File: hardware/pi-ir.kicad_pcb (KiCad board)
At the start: 2 copper layers, 56 x 35 mm, 10 parts, among them P1 RASPBERRYPI, P2 IROUT0, P3 IRIN, P4 IROUT1, U1 MOSFET-N, U2 MOSFET-N

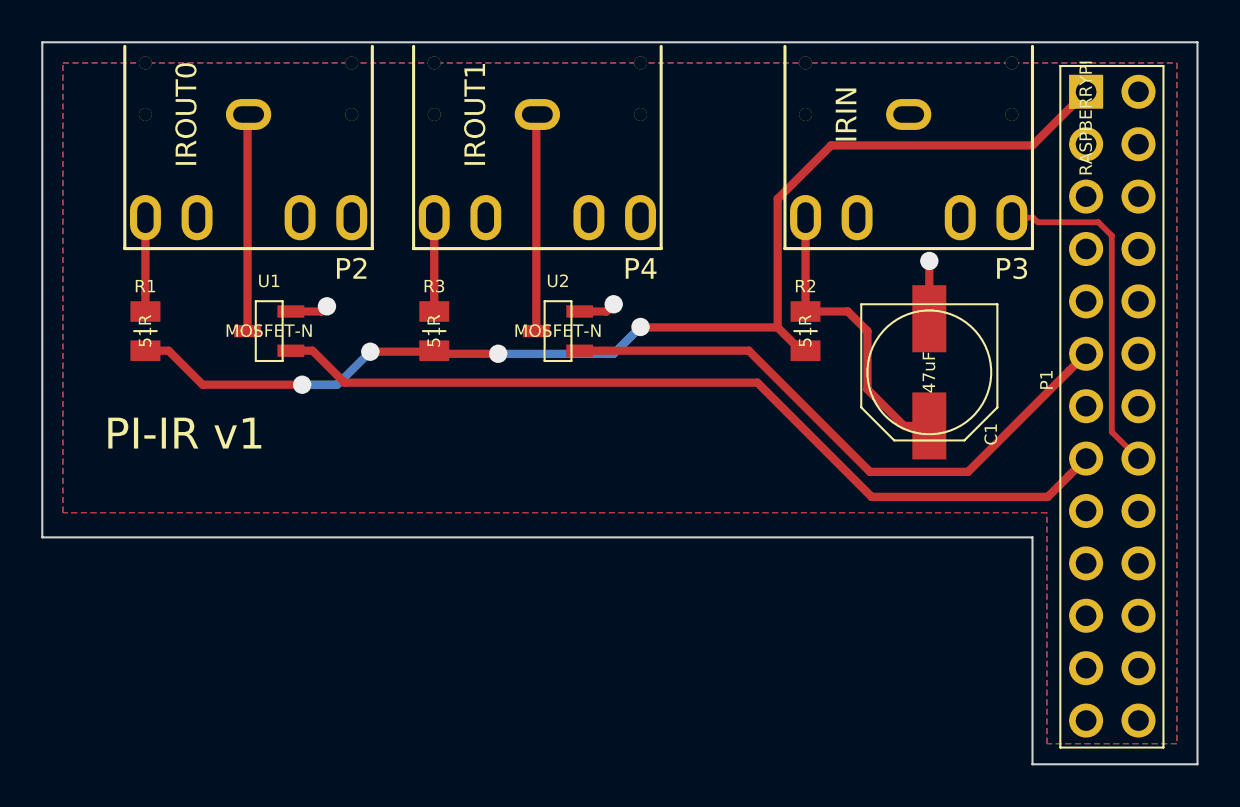
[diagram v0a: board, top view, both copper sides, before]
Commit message: add labels
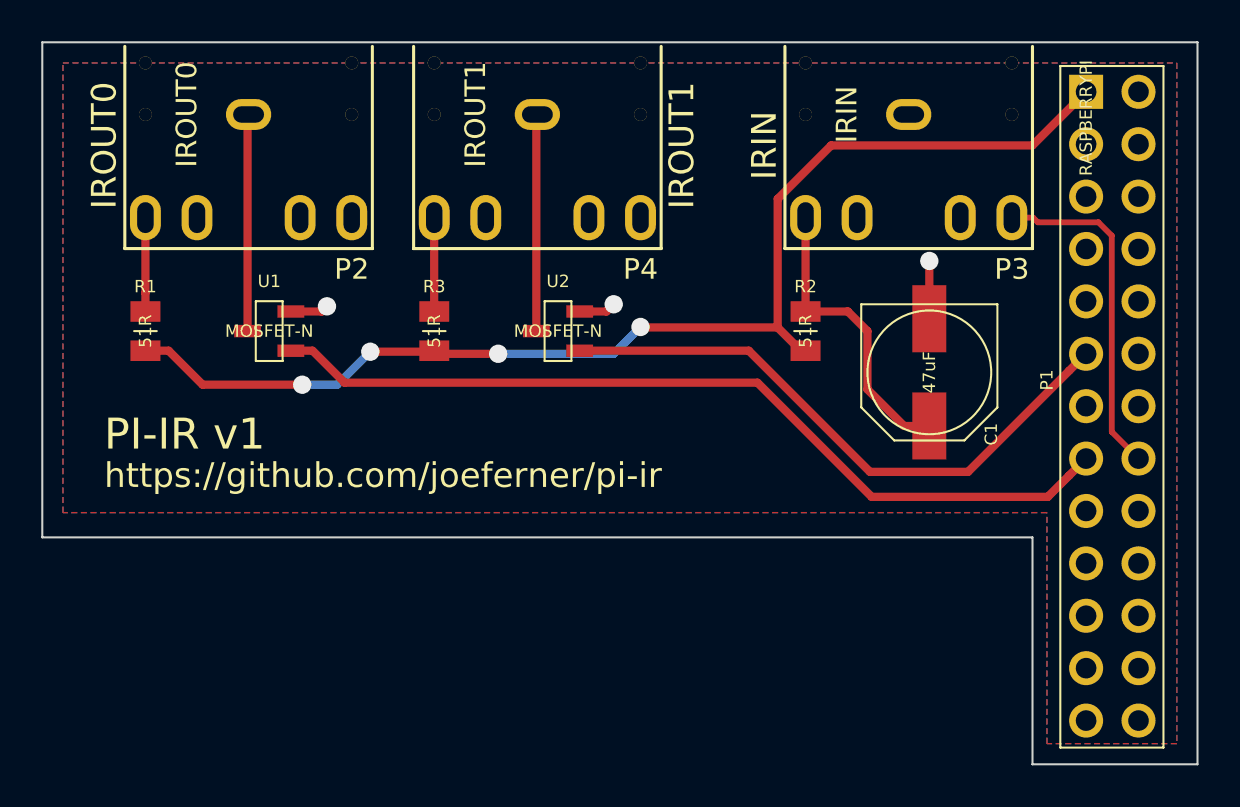
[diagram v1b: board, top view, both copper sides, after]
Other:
- board text added: "IRIN"
- board text added: "IROUT0"
- board text added: "IROUT1"
- board text added: "https://github.com/joeferner/pi-ir"

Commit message: initial v1 try
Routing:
- net +3.3V: track 57.8 -> 59.2 mm

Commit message: v1
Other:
- board text added: "By Joe Ferner"
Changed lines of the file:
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@@
     (area 99.949999 94.68 165.407144 135.050001)
     (thickness 1.6)
-    (drawings 13)
+    (drawings 14)
     (tracks 64)
     (zones 0)
@@
       (net 27 "Net-(P2-Pad2)"))
   )
+  (gr_text "By Joe Ferner" (at 123.6 118.6) (layer B.SilkS)
+    (effects (font (size 1.5 1.5) (thickness 0.3)) (justify mirror))
+  )
   (gr_text IRIN (at 135 105 90) (layer F.SilkS)

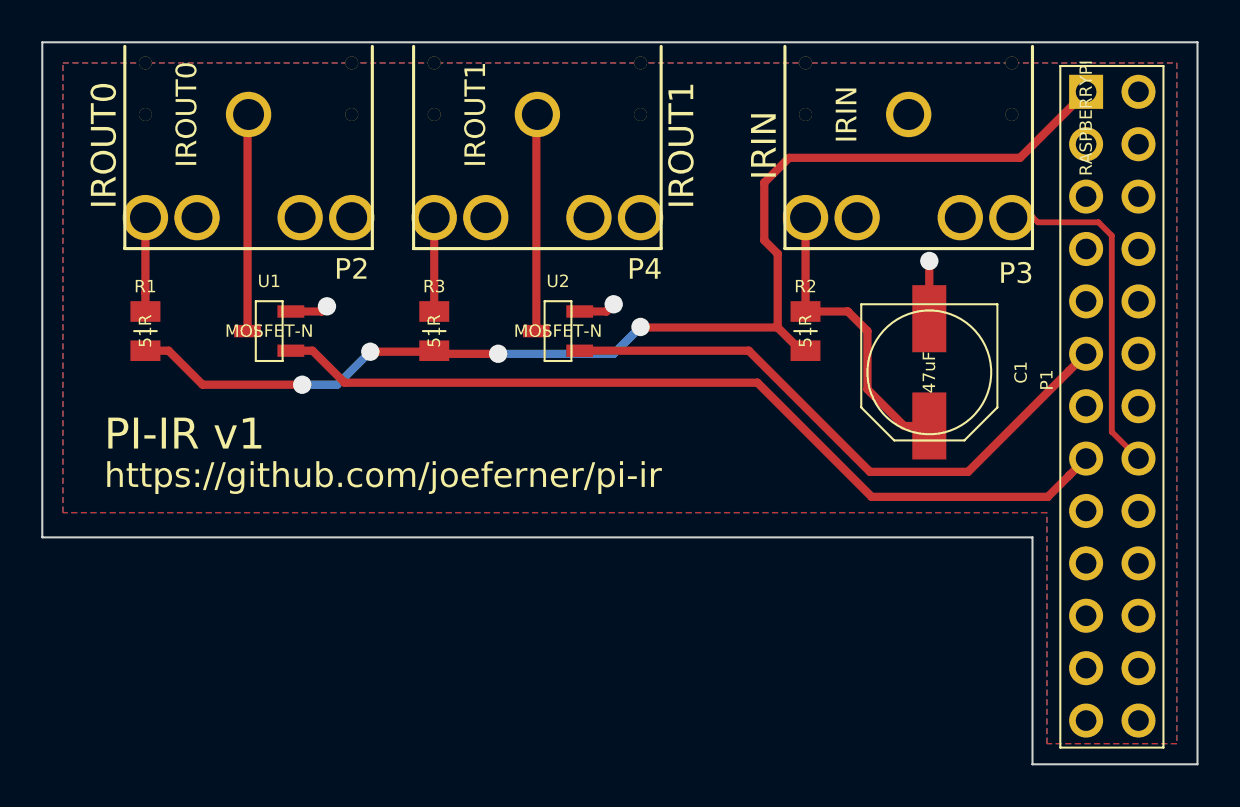
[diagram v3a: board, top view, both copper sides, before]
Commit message: add center hole to audio jack and try to fix drill
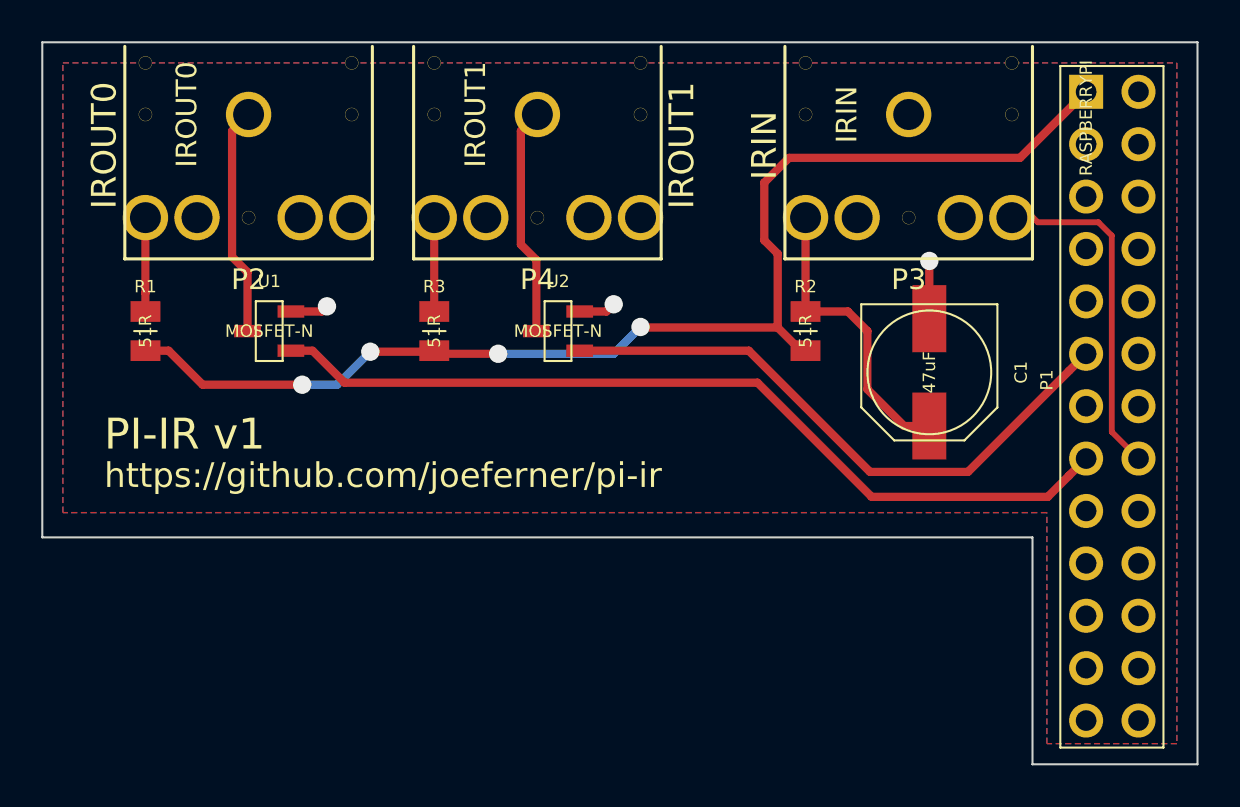
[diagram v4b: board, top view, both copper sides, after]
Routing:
- net Net-(P4-Pad1): track 10.5 -> 11.2 mm
- net Net-(P2-Pad1): track 10.5 -> 11.2 mm

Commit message: update kicad version
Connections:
- P1 pad 25: (no net) -> Net-(P1-Pad25)
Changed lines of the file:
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@@
-(kicad_pcb (version 3) (host pcbnew "(2014-05-22 BZR 4881)-product")
+(kicad_pcb (version 4) (host pcbnew "(2014-jul-16 BZR unknown)-product")
   (general
     (links 16)
@@
     (zones 0)
     (modules 10)
-    (nets 33)
+    (nets 34)
   )
   (page A4)
   (layers
-    (15 F.Cu signal)
-    (0 B.Cu signal)
-    (16 B.Adhes user)
-    (17 F.Adhes user)
-    (18 B.Paste user)
-    (19 F.Paste user)
-    (20 B.SilkS user)
-    (21 F.SilkS user)
-    (22 B.Mask user)
-    (23 F.Mask user)
-    (24 Dwgs.User user)
-    (25 Cmts.User user)
-    (26 Eco1.User user)
-    (27 Eco2.User user)
-    (28 Edge.Cuts user)
+    (0 F.Cu signal)
+    (31 B.Cu signal)
+    (32 B.Adhes user)
+    (33 F.Adhes user)
+    (34 B.Paste user)
+    (35 F.Paste user)
+    (36 B.SilkS user)
+    (37 F.SilkS user)
+    (38 B.Mask user)
+    (39 F.Mask user)
+    (40 Dwgs.User user)
+    (41 Cmts.User user)
+    (42 Eco1.User user)
+    (43 Eco2.User user)
+    (44 Edge.Cuts user)
   )
   (setup
@@
     (visible_elements FFFEFF7F)
     (pcbplotparams
-      (layerselection 284196865)
+      (layerselection 0x00030_80000001)
       (usegerberextensions true)
       (excludeedgelayer false)
@@
   (net 31 "Net-(P2-Pad3)")
   (net 32 "Net-(P4-Pad3)")
+  (net 33 "Net-(P1-Pad25)")
   (net_class Default "This is the default net class."
     (clearance 0.2032)
@@
     (add_net "Net-(P1-Pad23)")
     (add_net "Net-(P1-Pad24)")
+    (add_net "Net-(P1-Pad25)")
     (add_net "Net-(P1-Pad26)")
     (add_net "Net-(P1-Pad3)")
@@
     (pad 24 thru_hole circle (at 27.94 -2.54 270) (size 1.65 1.65) (drill 1) (layers *.Cu *.Mask F.SilkS)
       (net 25 "Net-(P1-Pad24)"))
-    (pad 25 thru_hole circle (at 30.48 0 270) (size 1.65 1.65) (drill 1) (layers *.Cu *.Mask F.SilkS))
+    (pad 25 thru_hole circle (at 30.48 0 270) (size 1.65 1.65) (drill 1) (layers *.Cu *.Mask F.SilkS)
+      (net 33 "Net-(P1-Pad25)"))
     (pad 26 thru_hole circle (at 30.48 -2.54 270) (size 1.65 1.65) (drill 1) (layers *.Cu *.Mask F.SilkS)
       (net 26 "Net-(P1-Pad26)"))
